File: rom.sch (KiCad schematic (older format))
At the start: 1 part, among them U6 ROM

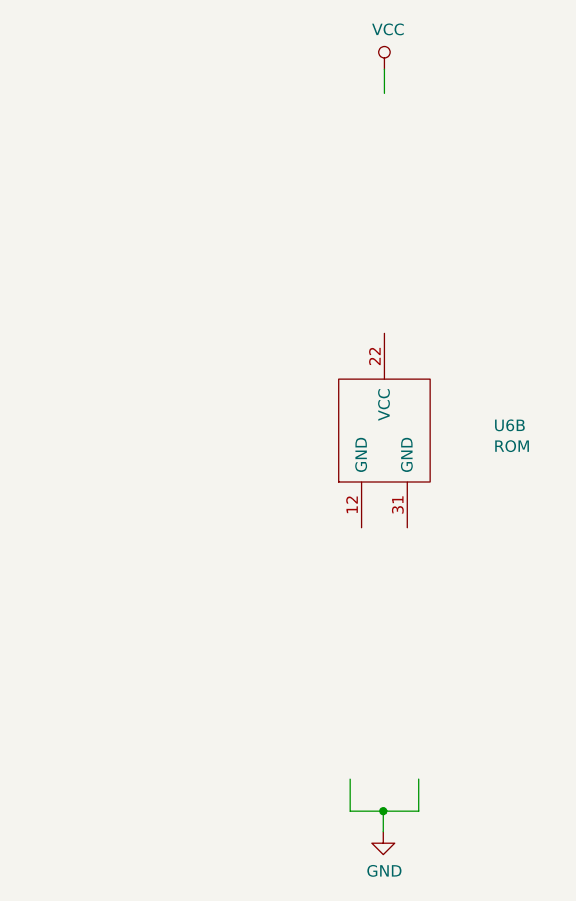
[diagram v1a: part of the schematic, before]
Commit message: Add power & decoupling, not yet complete
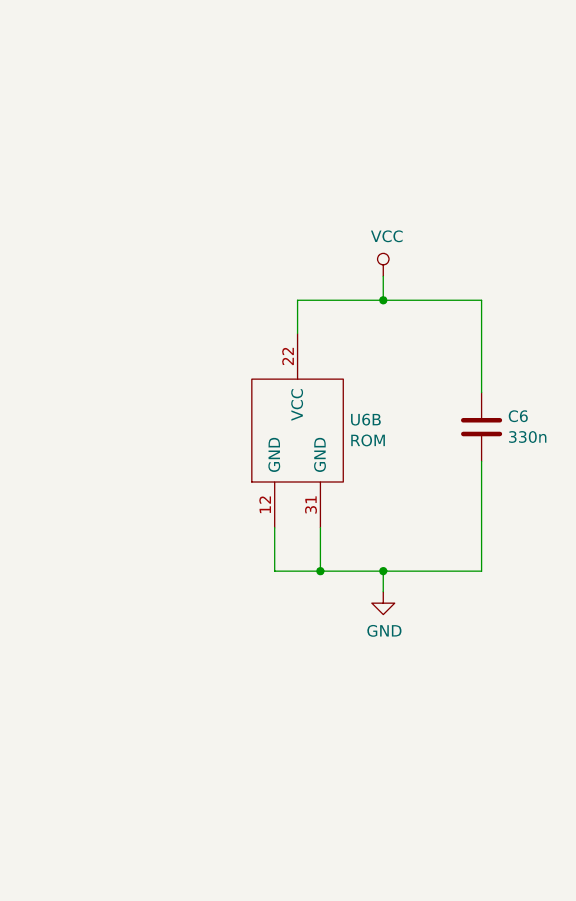
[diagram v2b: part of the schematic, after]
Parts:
- added C6: 330n, symbol Device:C
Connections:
- wire segments 47 -> 53
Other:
- moved on the sheet: U6B
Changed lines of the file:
@@
 $Descr A4 11693 8268
 encoding utf-8
-Sheet 9 11
+Sheet 9 12
 Title "Rämixx500"
 Date "2019-04-20"
@@
 L AMIGA_ROM:AMIGA_ROM U6
 U 2 1 5D8806F6
-P 8630 3585
-F 0 "U6" H 9108 3631 50  0000 L CNN
-F 1 "ROM" H 9108 3540 50  0000 L CNN
-F 2 "Package_DIP:DIP-42_W15.24mm_Socket_LongPads" H 8630 3585 50  0001 C CNN
-F 3 "DOCUMENTATION" H 8630 3585 50  0001 C CNN
-	2    8630 3585
-	1    0    0    -1
-$EndComp
-Wire Wire Line
-	8480 5085 8480 5225
-Wire Wire Line
-	8480 5225 8625 5225
-Wire Wire Line
-	8780 5225 8780 5085
+P 8250 3585
+F 0 "U6" H 8478 3656 50  0000 L CNN
+F 1 "ROM" H 8478 3565 50  0000 L CNN
+F 2 "Package_DIP:DIP-42_W15.24mm_Socket_LongPads" H 8250 3585 50  0001 C CNN
+F 3 "DOCUMENTATION" H 8250 3585 50  0001 C CNN
+	2    8250 3585
+	1    0    0    -1
+$EndComp
 $Comp
 L power:GND #PWR0198
 U 1 1 5D88175C
-P 8625 5315
-F 0 "#PWR0198" H 8625 5065 50  0001 C CNN
-F 1 "GND" H 8630 5142 50  0000 C CNN
-F 2 "" H 8625 5315 50  0001 C CNN
-F 3 "" H 8625 5315 50  0001 C CNN
-	1    8625 5315
-	1    0    0    -1
-$EndComp
-Wire Wire Line
-	8625 5315 8625 5225
-Connection ~ 8625 5225
-Wire Wire Line
-	8625 5225 8780 5225
+P 8625 4265
+F 0 "#PWR0198" H 8625 4015 50  0001 C CNN
+F 1 "GND" H 8630 4092 50  0000 C CNN
+F 2 "" H 8625 4265 50  0001 C CNN
+F 3 "" H 8625 4265 50  0001 C CNN
+	1    8625 4265
+	1    0    0    -1
+$EndComp
+Wire Wire Line
+	8625 4265 8625 4175
 $Comp
 L power:VCC #PWR0199
 U 1 1 5D8833DE
-P 8630 1980
-F 0 "#PWR0199" H 8630 1830 50  0001 C CNN
-F 1 "VCC" H 8647 2153 50  0000 C CNN
-F 2 "" H 8630 1980 50  0001 C CNN
-F 3 "" H 8630 1980 50  0001 C CNN
-	1    8630 1980
-	1    0    0    -1
-$EndComp
-Wire Wire Line
-	8630 2085 8630 1980
+P 8625 2885
+F 0 "#PWR0199" H 8625 2735 50  0001 C CNN
+F 1 "VCC" H 8642 3058 50  0000 C CNN
+F 2 "" H 8625 2885 50  0001 C CNN
+F 3 "" H 8625 2885 50  0001 C CNN
+	1    8625 2885
+	1    0    0    -1
+$EndComp
+Wire Wire Line
+	8625 2990 8625 2885
+$Comp
+L Device:C C6
+U 1 1 5E9EA8DA
+P 9055 3545
+F 0 "C6" H 9170 3591 50  0000 L CNN
+F 1 "330n" H 9170 3500 50  0000 L CNN
+F 2 "" H 9093 3395 50  0001 C CNN
+F 3 "~" H 9055 3545 50  0001 C CNN
+	1    9055 3545
+	1    0    0    -1
+$EndComp
+Wire Wire Line
+	8250 3135 8250 2990
+Wire Wire Line
+	8250 2990 8625 2990
+Wire Wire Line
+	9055 2990 9055 3395
+Wire Wire Line
+	9055 3695 9055 4175
+Wire Wire Line
+	9055 4175 8625 4175
+Wire Wire Line
+	8150 4175 8150 3985
+Wire Wire Line
+	8350 3985 8350 4175
+Connection ~ 8350 4175
+Wire Wire Line
+	8350 4175 8150 4175
+Connection ~ 8625 4175
+Wire Wire Line
+	8625 4175 8350 4175
+Connection ~ 8625 2990
+Wire Wire Line
+	8625 2990 9055 2990
 Wire Bus Line
 	6530 1930 6530 4485

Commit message: Fix power-up reset
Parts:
- C6: footprint (none) -> Raemixx500:C_Axial_L6.3mm_D2.5mm_P10.16mm
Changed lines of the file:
@@
 EESchema Schematic File Version 4
 LIBS:Raemix500-cache
-EELAYER 26 0
+EELAYER 29 0
 EELAYER END
 $Descr A4 11693 8268
@@
 F 0 "C6" H 9170 3591 50  0000 L CNN
 F 1 "330n" H 9170 3500 50  0000 L CNN
-F 2 "" H 9093 3395 50  0001 C CNN
+F 2 "Raemixx500:C_Axial_L6.3mm_D2.5mm_P10.16mm" H 9093 3395 50  0001 C CNN
 F 3 "~" H 9055 3545 50  0001 C CNN
 	1    9055 3545
